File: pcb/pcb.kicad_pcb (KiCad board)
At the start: 2 copper layers, 238.1 x 94.6 mm, 70 parts, among them SW1 SW_PUSH, SW10 SW_PUSH, SW11 SW_PUSH, SW12 SW_PUSH, SW13 SW_PUSH, SW14 SW_PUSH, SW15 SW_PUSH, SW16 SW_PUSH, SW17 SW_PUSH, SW18 SW_PUSH, SW19 SW_PUSH, SW2 SW_PUSH, SW20 SW_PUSH, SW21 SW_PUSH, SW22 SW_PUSH, SW23 SW_PUSH, SW24 SW_PUSH, SW25 SW_PUSH, SW26 SW_PUSH, SW27 SW_PUSH, SW28 SW_PUSH, SW29 SW_PUSH, SW3 SW_PUSH, SW30 SW_PUSH, SW31 SW_PUSH, SW32 SW_PUSH, SW33 Rotary_Encoder_Switch, SW34 SW_PUSH, SW4 SW_PUSH, SW5 SW_PUSH, SW6 SW_PUSH, SW7 SW_PUSH, SW8 SW_PUSH, SW9 SW_PUSH, U1 ProMicro

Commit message: Finishes move back to pro micro, adds silk footprint and lib, updates routing, fixes outline
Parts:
- moved R1 6.35 mm to (129.0, 124.0), turned to 270 degrees
- moved R2 4.24 mm to (133.0, 124.0), turned to 270 degrees
- moved SW33 1.32 mm to (144.7, 97.2)
- moved OL1 1.28 mm to (148.1, 125.2)
- moved U1 0.51 mm to (144.7, 71.5)
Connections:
- U1 pad 12: ROW0 -> COL0
- U1 pad 24: Net-(U1-Pad24) -> (no net)
- U1 pad 7: COL0 -> ROW0
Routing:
- net GND: track 114.5 -> 18.8 mm, vias 1 -> 0
- net COL6: track 116.0 -> 76.7 mm, vias 2 -> 1
- net COL7: track 135.3 -> 99.0 mm, vias 2 -> 1
- net COL8: track 154.3 -> 119.5 mm, vias 2 -> 1
- net COL2: track 140.7 -> 106.1 mm
- net COL9: track 174.7 -> 142.6 mm, vias 2 -> 0
- net COL0: track 177.5 -> 149.7 mm
- net COL1: track 161.3 -> 134.0 mm, vias 2 -> 0
- net COL3: track 113.7 -> 87.4 mm, vias 2 -> 1
- net COL4: track 141.6 -> 118.2 mm, vias 3 -> 0
- net ROW2: track 259.1 -> 242.5 mm
- net ROW3: track 105.2 -> 89.9 mm, vias 2 -> 0
- net SCL: track 87.8 -> 76.7 mm, vias 2 -> 1
- net ROW1: track 234.0 -> 223.6 mm
- net ROW0: track 229.5 -> 221.9 mm, vias 2 -> 0
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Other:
- board size 238.1 x 94.6 mm -> 234.6 x 93.6 mm

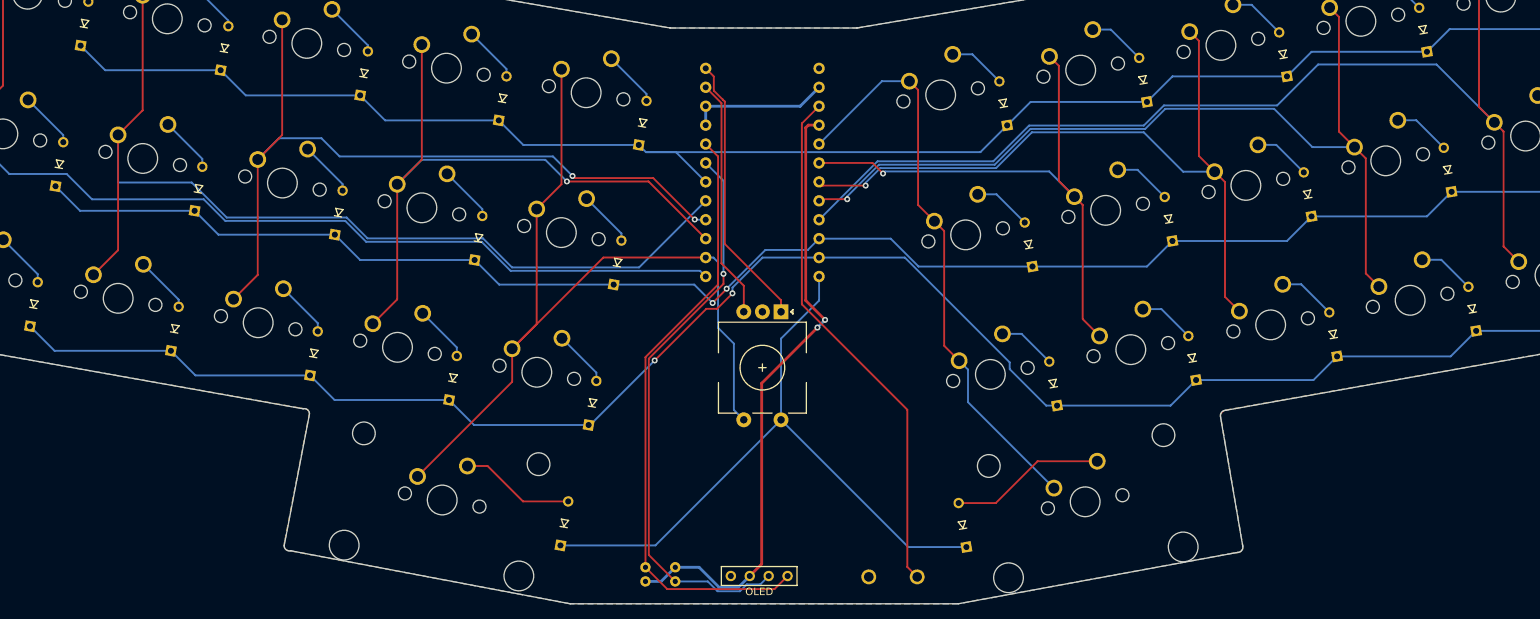
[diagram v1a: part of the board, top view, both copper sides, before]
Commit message: Adds m2 holes, adds updated gerbers
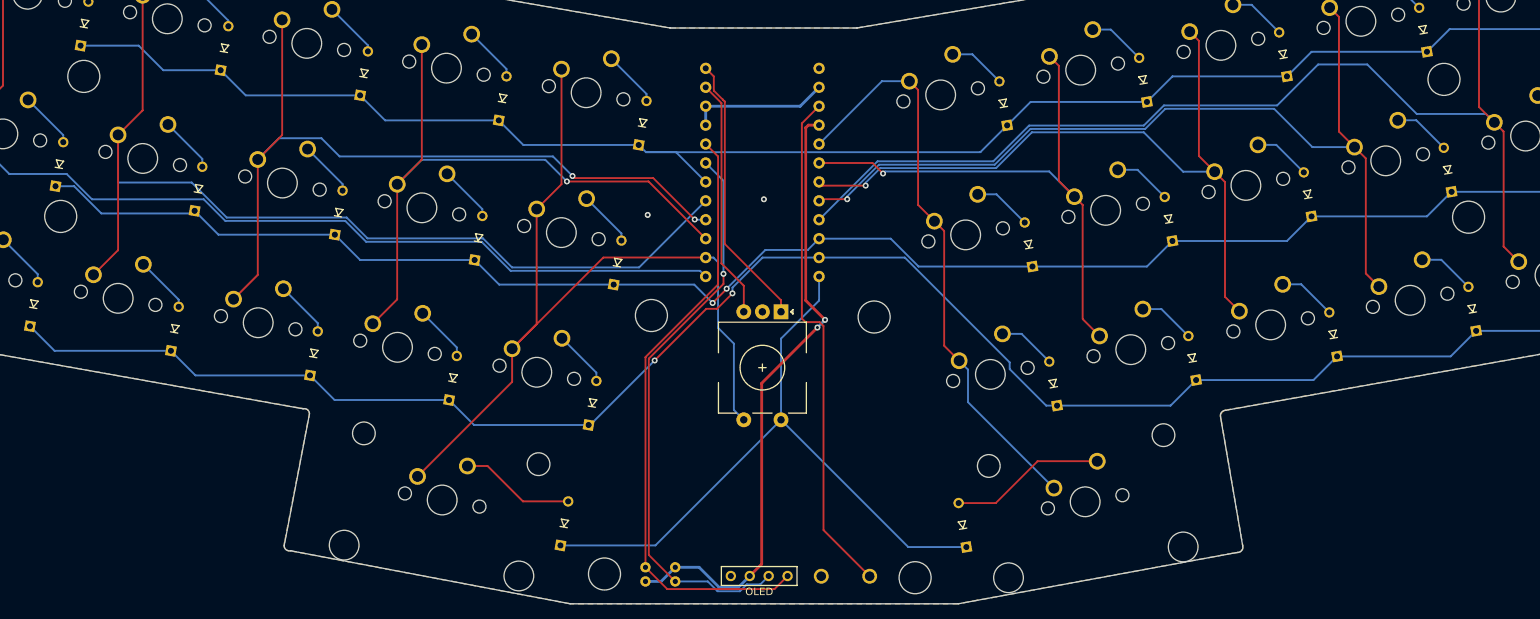
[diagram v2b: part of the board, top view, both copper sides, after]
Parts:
- added Ref**: Val**, kbd:M2_HOLE_v2, F.Cu at (123.5, 124.9)
- added Ref**: Val**, kbd:M2_HOLE_v2, F.Cu at (165.2, 125.4)
- added Ref**: Val**, kbd:M2_HOLE_v2, F.Cu at (129.8, 90.2)
- added Ref**: Val**, kbd:M2_HOLE_v2, F.Cu at (159.7, 90.4)
- added Ref**: Val**, kbd:M2_HOLE_v2, F.Cu at (50.5, 76.9)
- added Ref**: Val**, kbd:M2_HOLE_v2, F.Cu at (53.6, 58.1)
- added Ref**: Val**, kbd:M2_HOLE_v2, F.Cu at (236.2, 58.5)
- added Ref**: Val**, kbd:M2_HOLE_v2, F.Cu at (239.5, 77.0)
- moved SW34 6.38 mm to (155.8, 125.2)
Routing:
- net reset: track 70.6 -> 68.9 mm
- net GND: vias 0 -> 2
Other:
- rule pad_to_mask_clearance: 0.051 -> 0

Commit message: Updates for silk
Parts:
- added G***: LOGO, kawa:kawa_silk, B.Cu at (144.9, 106.8)
- added G***: LOGO, kawa:kawa_silk, B.Cu at (144.8, 70.4)
- added G***: LOGO, kawa:kawa_silk, B.Cu at (110.3, 88.5)
- added G***: LOGO, kawa:kawa_silk, B.Cu at (179.4, 88.2)
- added G***: LOGO, kawa:kawa_silk, F.Cu at (110.2, 88.6)
- added G***: LOGO, kawa:kawa_silk, F.Cu at (179.3, 88.9)
- added G***: LOGO, kawa:kawa_silk, F.Cu at (144.7, 106.7)
- added G***: LOGO, kawa:kawa_silk, F.Cu at (144.8, 70.3)

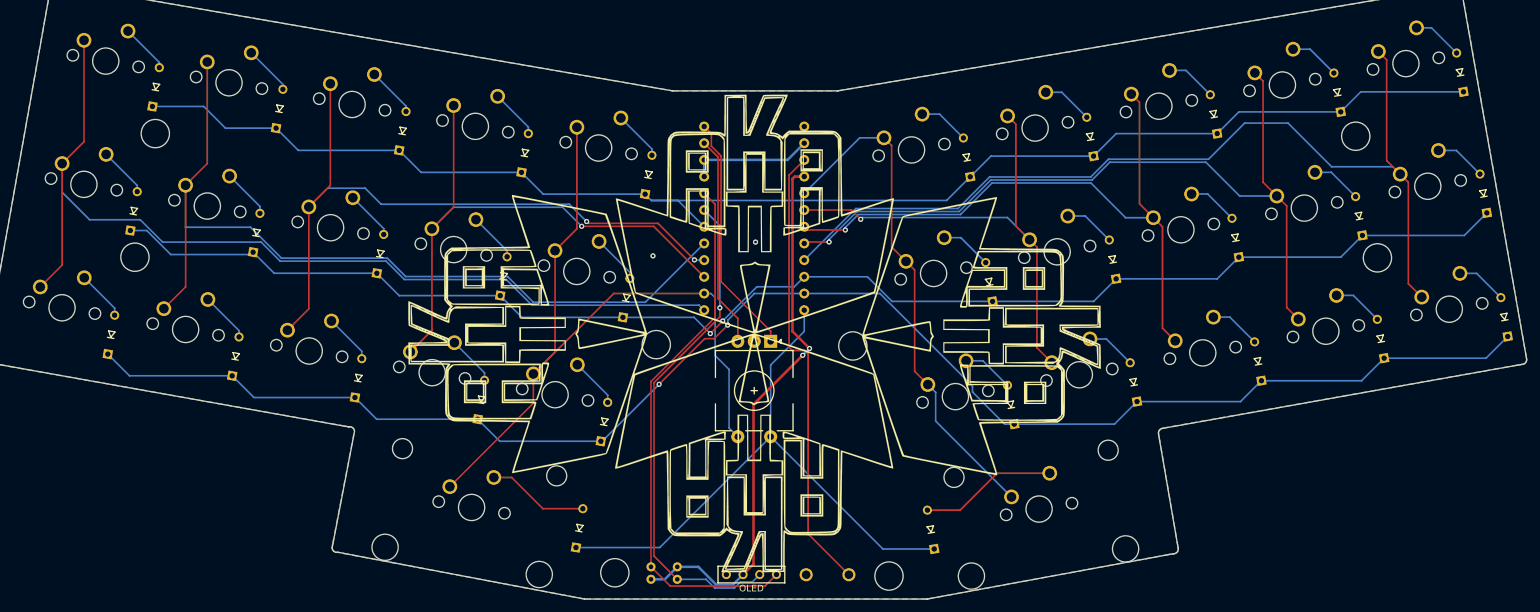
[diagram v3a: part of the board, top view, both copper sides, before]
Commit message: Updates kawa to remove encoder, adds new oled footprint, reroute accordingly
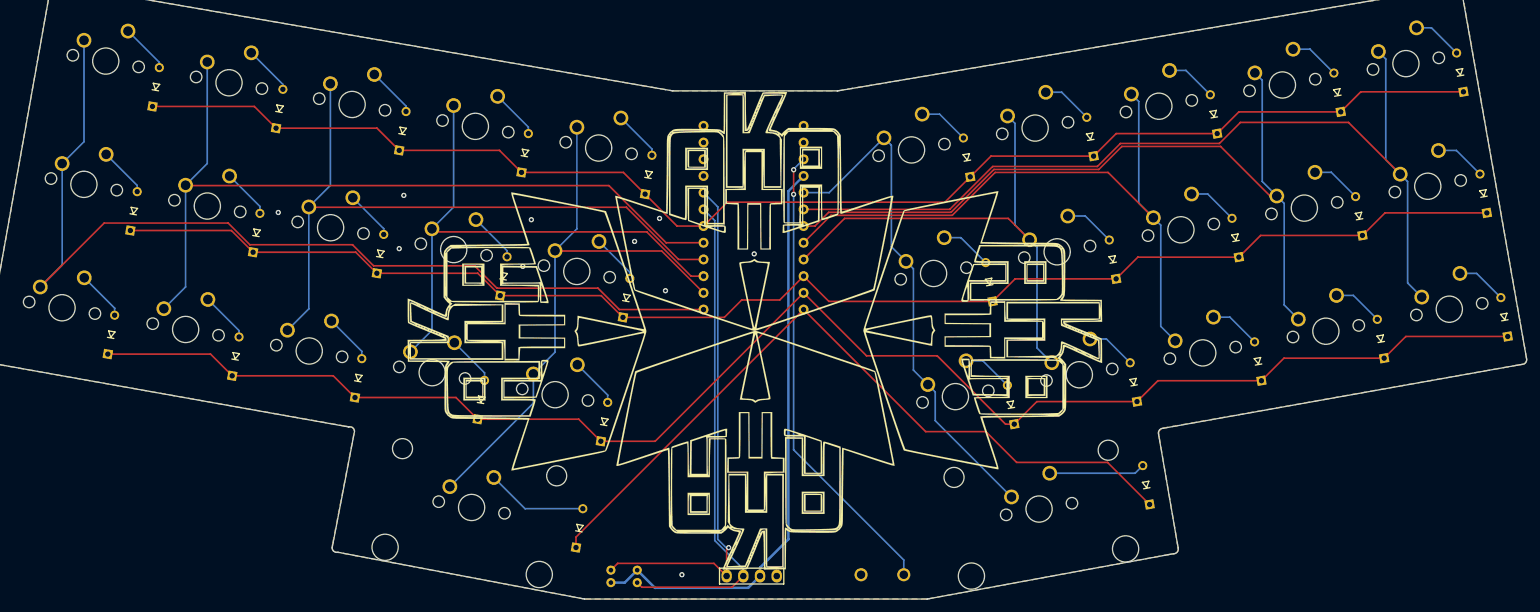
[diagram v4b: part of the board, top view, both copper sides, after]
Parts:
- removed the G*** at (144.9, 106.8)
- removed the G*** at (144.8, 70.4)
- removed the G*** at (110.3, 88.5)
- removed the G*** at (179.4, 88.2)
- removed the G*** at (110.2, 88.6)
- removed the G*** at (179.3, 88.9)
- removed the G*** at (144.7, 106.7)
- removed the G*** at (144.8, 70.3)
- removed OL1: OLED, kbd:OLED_1side
- removed Ref** (x8): Val**, kbd:M2_HOLE_v2
- removed SW33: Rotary_Encoder_Switch, keebio-parts:RotaryEncoder_EC11
- added Brd1: SSD1306, SSD1306:128x64OLED, F.Cu at (144.5, 114.8)
- added G***: LOGO, kawa:kawa_silk, B.Cu at (144.7, 106.1)
- added G***: LOGO, kawa:kawa_silk, B.Cu at (144.9, 69.7)
- added G***: LOGO, kawa:kawa_silk, B.Cu at (110.1, 87.8)
- added G***: LOGO, kawa:kawa_silk, B.Cu at (179.5, 88.0)
- added G***: LOGO, kawa:kawa_silk, F.Cu at (110.1, 88.2)
- added G***: LOGO, kawa:kawa_silk, F.Cu at (179.5, 88.0)
- added G***: LOGO, kawa:kawa_silk, F.Cu at (144.9, 106.3)
- added G***: LOGO, kawa:kawa_silk, F.Cu at (144.7, 69.9)
- moved D32 33.5 mm to (204.3, 111.6)
- moved SW34 8.35 mm to (164.2, 125.2)
- moved R1 6.12 mm to (122.9, 124.5)
- moved R2 6.12 mm to (126.9, 124.5)
- moved U1 0.14 mm to (144.6, 71.4)
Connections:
- U1 pad 1: S0 -> (no net)
- U1 pad 16: COL9 -> COL6
- U1 pad 17: COL8 -> COL7
- U1 pad 18: COL7 -> COL8
- U1 pad 19: COL6 -> COL9
- U1 pad 2: S1 -> (no net)
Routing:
- net S0: track 36.9 -> 0.00 mm
- net S1: track 32.3 -> 0.00 mm
- net COL4: track 118.2 -> 87.9 mm
- net ROW3: track 89.9 -> 115.5 mm
- net GND: track 18.8 -> 0.00 mm, vias 2 -> 10
- net COL1: track 134.0 -> 122.7 mm
- net ROW0: track 221.9 -> 215.4 mm
- net Net-(D32-Pad2): track 20.9 -> 14.6 mm
- net VCC: track 83.9 -> 88.9 mm, vias 2 -> 0
- net SDA: track 82.6 -> 79.2 mm, vias 0 -> 1
- net COL9: track 142.6 -> 139.6 mm
- net COL3: track 87.4 -> 84.5 mm, vias 1 -> 0
- net COL2: track 106.1 -> 103.5 mm, vias 2 -> 0
- net ROW1: track 223.9 -> 221.6 mm, vias 2 -> 0
- net COL6: track 76.7 -> 78.7 mm, vias 1 -> 0
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
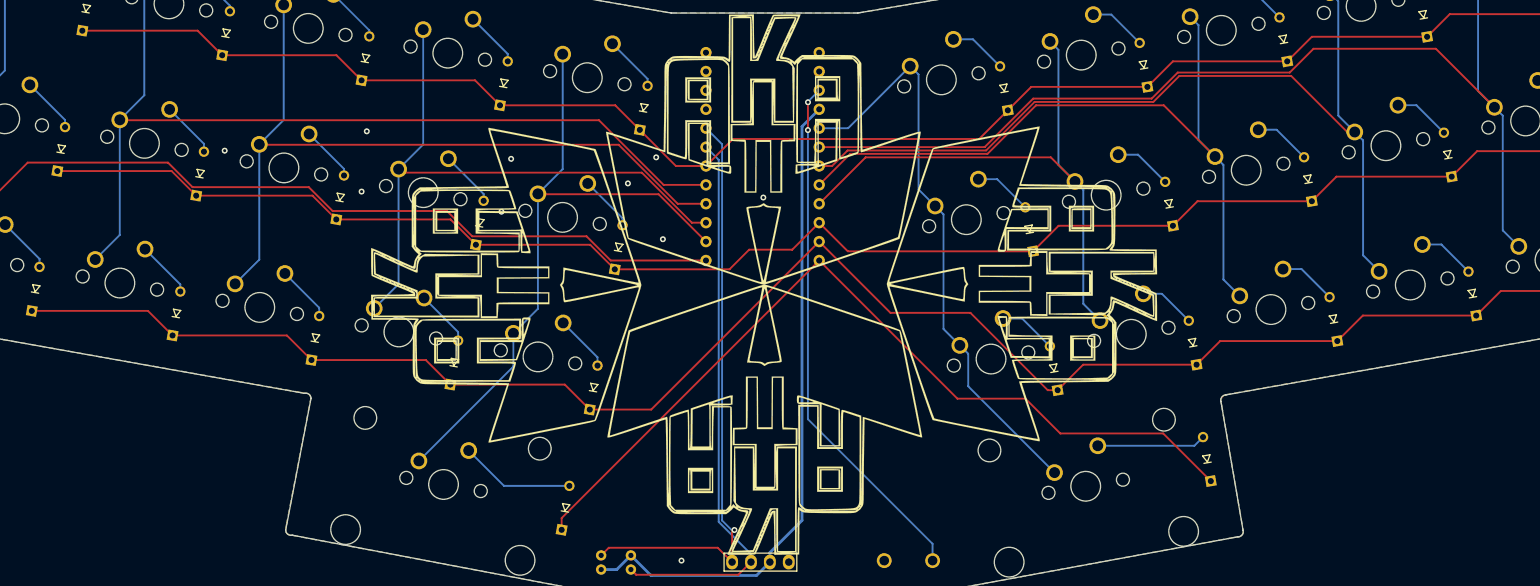
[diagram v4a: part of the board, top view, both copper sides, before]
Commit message: Updates kawa gerbers with m2 holes
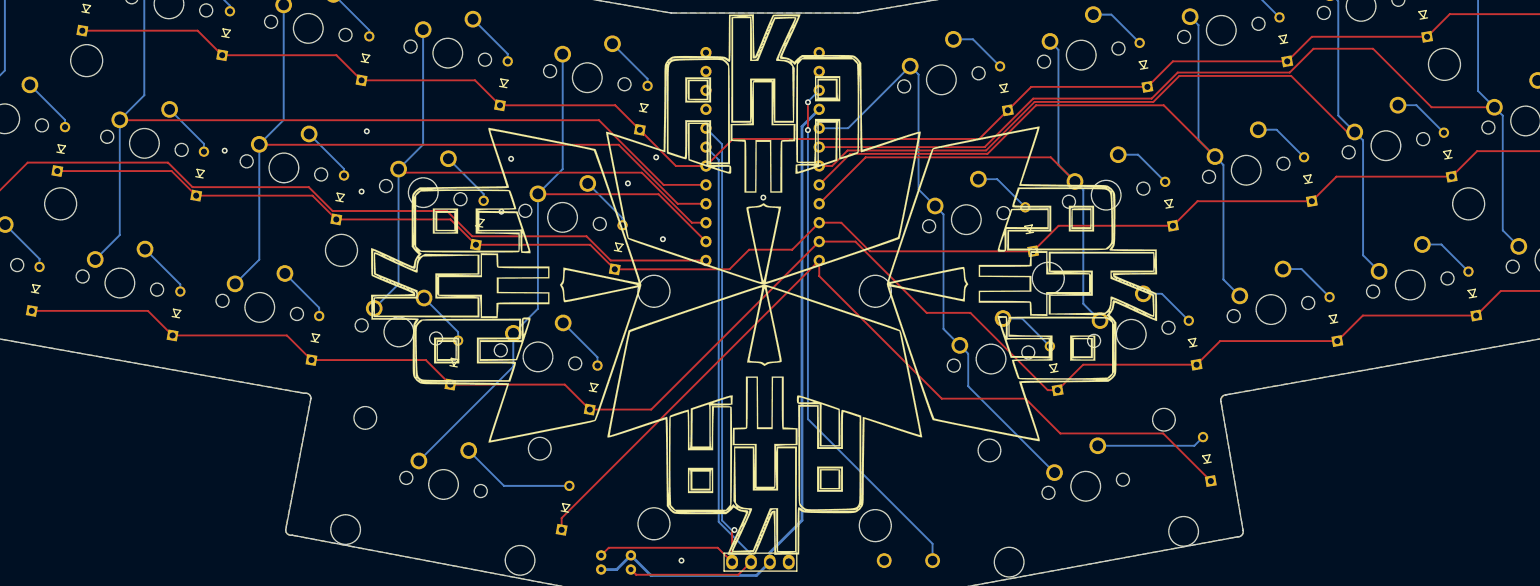
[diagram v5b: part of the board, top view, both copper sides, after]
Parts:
- added Ref**: Val**, kbd:M2_HOLE_v2, F.Cu at (183.0, 87.2)
- added Ref**: Val**, kbd:M2_HOLE_v2, F.Cu at (130.0, 120.2)
- added Ref**: Val**, kbd:M2_HOLE_v2, F.Cu at (88.0, 83.5)
- added Ref**: Val**, kbd:M2_HOLE_v2, F.Cu at (239.5, 77.2)
- added Ref**: Val**, kbd:M2_HOLE_v2, F.Cu at (236.2, 58.5)
- added Ref**: Val**, kbd:M2_HOLE_v2, F.Cu at (50.2, 77.2)
- added Ref**: Val**, kbd:M2_HOLE_v2, F.Cu at (53.8, 58.0)
- added Ref**: Val**, kbd:M2_HOLE_v2, F.Cu at (159.8, 89.0)
- added Ref**: Val**, kbd:M2_HOLE_v2, F.Cu at (130.0, 89.0)
- added Ref**: Val**, kbd:M2_HOLE_v2, F.Cu at (159.8, 120.5)
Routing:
- net ROW3: track 115.5 -> 116.7 mm
